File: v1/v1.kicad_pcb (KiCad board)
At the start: 2 copper layers, 50.4 x 44 mm, 54 parts, among them J1 USB_C_Receptacle_USB2.0_16P, Q1 FS8205A, U1 DW01A, U2 MCP73871-2CC, U3 TPS63000, U4 USBLC6-2SC6, U5 SI1016X-T1-GE3, U6 ESP32-WROOM-E, U7 CH340N, Y1 32.768khz

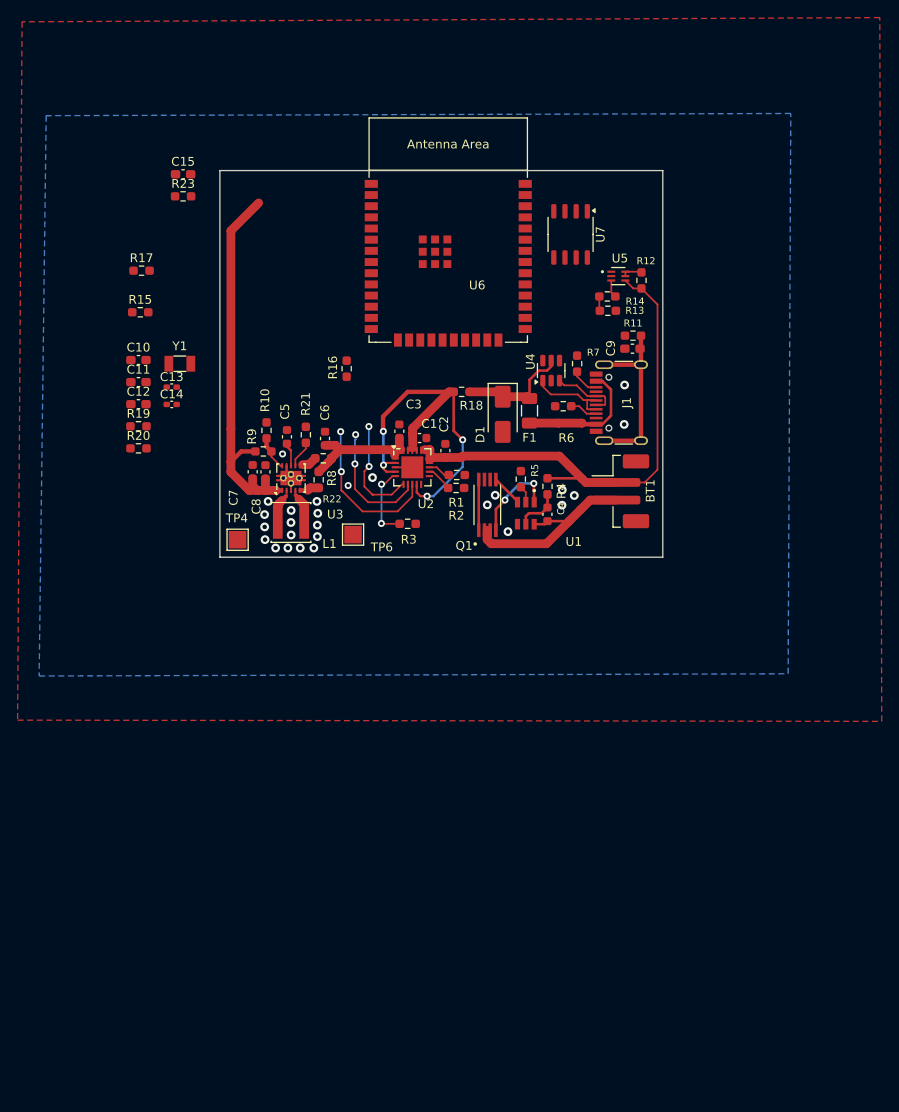
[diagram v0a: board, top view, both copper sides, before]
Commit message: Updated layout
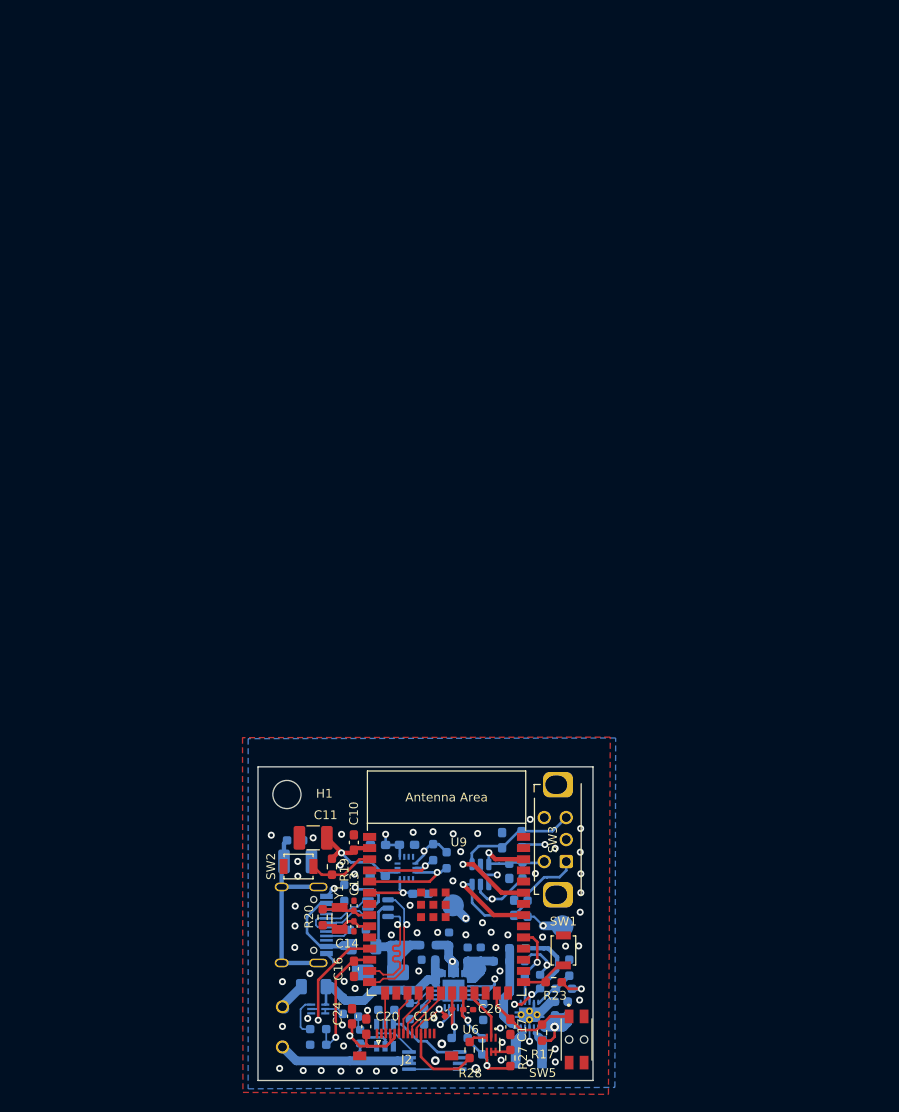
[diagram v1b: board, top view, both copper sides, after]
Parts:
- removed TP4: 3.3v, TestPoint:TestPoint_Pad_2.0x2.0mm
- removed TP6: USB_BAT_AUTO, TestPoint:TestPoint_Pad_2.0x2.0mm
- added C16: 0.1uf, Capacitor_SMD:C_0603_1608Metric_Pad1.08x0.95mm_HandSolder, F.Cu at (115.8, 146.7)
- added C17: 0.1uf, Capacitor_SMD:C_0603_1608Metric_Pad1.08x0.95mm_HandSolder, F.Cu at (133.6, 153.3)
- added C18: 0.1uf, Capacitor_SMD:C_0603_1608Metric_Pad1.08x0.95mm_HandSolder, B.Cu at (133.4, 135.6)
- added C19: 0.1uf, Capacitor_SMD:C_0402_1005Metric_Pad0.74x0.62mm_HandSolder, F.Cu at (126.6, 151.7)
- added C20: 10uf, Capacitor_SMD:C_0603_1608Metric_Pad1.08x0.95mm_HandSolder, F.Cu at (115.6, 152.1)
- added C21: 10uf, Capacitor_SMD:C_0603_1608Metric_Pad1.08x0.95mm_HandSolder, B.Cu at (118.5, 136.2)
- added C22: 0.1uf, Capacitor_SMD:C_0603_1608Metric_Pad1.08x0.95mm_HandSolder, B.Cu at (121.8, 132.6)
- added C23: 0.1uf, Capacitor_SMD:C_0603_1608Metric_Pad1.08x0.95mm_HandSolder, B.Cu at (118.5, 132.7)
- added C24: 0.1uf, Capacitor_SMD:C_0603_1608Metric_Pad1.08x0.95mm_HandSolder, F.Cu at (117.2, 153.3)
- added C25: 0.1uf, Capacitor_SMD:C_0603_1608Metric_Pad1.08x0.95mm_HandSolder, B.Cu at (123.4, 138.2)
- added C26: 0.1uf, Capacitor_SMD:C_0402_1005Metric_Pad0.74x0.62mm_HandSolder, F.Cu at (128.8, 151.4)
- added F2: 1.5A 1206L150THWR, Fuse:Fuse_1206_3216Metric, B.Cu at (111.2, 148.8)
- added G1: GND_TP, TestPoint:TestPoint_Pad_D2.5mm, B.Cu at (127.0, 139.5)
- added H1: MountingHole, MountingHole:MountingHole_3.2mm_M3_ISO14580, F.Cu at (108.2, 126.9)
- added J2: GMT177 Display, Connector_FFC-FPC:TE_1-1734839-3_1x13-1MP_P0.5mm_Horizontal, F.Cu at (121.6, 155.4)
- added P1: 3.3V TP, TestPoint:TestPoint_Pad_D2.5mm, B.Cu at (139.5, 141.9)
- added R24: 10k, Resistor_SMD:R_0603_1608Metric_Pad0.98x0.95mm_HandSolder, B.Cu at (135.5, 139.9)
- added R25: 10k, Resistor_SMD:R_0603_1608Metric_Pad0.98x0.95mm_HandSolder, B.Cu at (134.8, 132.0)
- added R26: 10k, Resistor_SMD:R_0603_1608Metric_Pad0.98x0.95mm_HandSolder, B.Cu at (134.9, 135.6)
- added R27: 10k, Resistor_SMD:R_0603_1608Metric_Pad0.98x0.95mm_HandSolder, F.Cu at (133.6, 156.9)
- added R28: 10, Resistor_SMD:R_0603_1608Metric_Pad0.98x0.95mm_HandSolder, F.Cu at (128.9, 156.0)
- added R29: 10k, Resistor_SMD:R_0603_1608Metric_Pad0.98x0.95mm_HandSolder, B.Cu at (126.3, 134.4)
- added R30: 10k, Resistor_SMD:R_0603_1608Metric_Pad0.98x0.95mm_HandSolder, B.Cu at (124.8, 133.5)
- added SW1: SW_Push, Button_Switch_SMD:SW_SPST_B3U-1000P, F.Cu at (139.6, 144.7)
- added SW2: SW_Push, Button_Switch_SMD:SW_SPST_B3U-1000P, F.Cu at (109.5, 135.1)
- added SW3: RotaryEncoder_Switch, Rotary_Encoder:RotaryEncoder_Bourns_Horizontal_PEC12R-2x17F-Sxxxx, F.Cu at (139.9, 134.5)
- added SW5: Back button, Right angle switch:EVQPUC02K, F.Cu at (141.1, 154.8)
- added U8: BMI270, Package_LGA:Bosch_LGA-14_3x2.5mm_P0.5mm, B.Cu at (121.8, 135.3)
- added U9: ESP32-S3-WROOM-1, PCM_Espressif:ESP32-S3-WROOM-1, F.Cu at (126.3, 140.0)
- BT1: footprint Connector_JST:JST_PH_B2B-PH-SM4-TB_1x02-1MP_P2.00mm_Vertical -> Battery_Library:4.2v_battery_mount; moved to B.Cu
- C1, C12, C15, C2, C3, C4, C5, C6, C7, C8, D1, J1, L1, Q1, R1, R10, R11, R12, R13, R14, R15, R16, R2, R21, R3, R4, R5, R6, R7, R8, R9, U1, U2, U3, U4, U5: moved to B.Cu
- C11: footprint Capacitor_SMD:C_0603_1608Metric_Pad1.08x0.95mm_HandSolder -> Capacitor_SMD:C_1210_3225Metric_Pad1.33x2.70mm_HandSolder
- C9: footprint Capacitor_SMD:C_0603_1608Metric_Pad1.08x0.95mm_HandSolder -> Capacitor_SMD:C_1210_3225Metric_Pad1.33x2.70mm_HandSolder; moved to B.Cu
- F1: value 1A 1206L050YR -> 1.5A 1206L150THWR; moved to B.Cu
- R17: value 100k -> 10k
- R18, R22: value 0.1 -> 0; moved to B.Cu
- U6: value ESP32-WROOM-E -> SI1016X-T1-GE3; footprint PCM_Espressif:ESP32-WROOM-32E -> footprints:SOT_X-T1-GE3_VIS-M
- U7: value CH340N -> SRV05-4; footprint Package_SO:SOP-8_3.9x4.9mm_P1.27mm -> Package_TO_SOT_SMD:SOT-23-6; moved to B.Cu
- moved R23 98.8 mm to (138.5, 148.3)
- moved R17 97.9 mm to (137.2, 154.0), turned to 90 degrees
- moved R15 92.1 mm to (130.4, 155.6), turned to 90 degrees
- moved C15 91.5 mm to (134.0, 139.8), turned to 90 degrees
- moved U6 91.0 mm to (131.4, 155.4), turned to -90 degrees
- moved U5 90.0 mm to (111.7, 151.3)
- moved R13 89.7 mm to (111.7, 155.4), turned to 180 degrees
- moved R14 89.5 mm to (111.7, 153.6), turned to 0 degrees
- moved R12 89.2 mm to (114.5, 151.0), turned to -90 degrees
- moved R16 77.2 mm to (127.8, 154.6), turned to 180 degrees
- moved U7 73.5 mm to (130.2, 136.0)
- moved BT1 71.8 mm to (107.7, 153.1), turned to 90 degrees
- moved J1 70.9 mm to (108.6, 141.8)
- moved C7 70.7 mm to (140.1, 151.2)
- moved R10 70.1 mm to (140.3, 146.6)
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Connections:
- net /Power Module/BATT_LIFE_DATA_ANALOG renamed /MCU/BATT_READ_DATA_ANALOG
- net /Power Module/GPIO_BUCK_BOOST_PS_EN renamed /MCU/PWR_EFFICIENCY_MODE
- BT1 pad 1: /Power Module/B+ -> /Power Module/B-
- BT1 pad 2: /Power Module/B- -> Net-(BT1-+)
- C12 pad 1: Net-(U6-EN/CHIP_PU) -> /MCU/ROTARY_B
- C15 pad 1: GND -> /MCU/ROTARY_A
- C15 pad 2: Net-(U7-V3) -> GND
- D1 pad 1: /MCU/USB_5V -> /Power Module/USB_5V_FUSE_PROT
- F1 pad 2: /MCU/USB_5V -> /Power Module/USB_5V_FUSE_PROT
- R17 pad 2: /Power Module/STAT2 -> Net-(U9-GPIO48/SPICLK_N/SUBSPICLK_N_DIFF)
- R18 pad 1: /MCU/USB_5V -> /Power Module/USB_5V_FUSE_PROT
- R19 pad 2: Net-(U6-EN/CHIP_PU) -> Net-(U9-EN)
- R22 pad 1: /Power Module/AUTO_SWTCH_5V -> /Power Module/AUTO_PATH_PWR
- R22 pad 2: Net-(U3-VIN) -> /Power Module/AUTO_SWTCH_5V
- R23 pad 1: /Power Module/3.3V_PWR -> Net-(U9-GPIO0/BOOT)
- R23 pad 2: Net-(U6-GPIO0/BOOT/ADC2_CH1) -> /Power Module/3.3V_PWR
- R8 pad 1: /Power Module/AUTO_SWTCH_5V -> Net-(U3-EN)
- R8 pad 2: Net-(U3-EN) -> /Power Module/AUTO_PATH_PWR
- U3 pad 5: Net-(U3-VIN) -> /Power Module/AUTO_PATH_PWR
- U4 pad 5: /MCU/USB_5V -> /Power Module/USB_5V_FUSE_PROT
- U5 pad 2: /Power Module/BATT_LIFE_READ_EN -> /MCU/BAT_READ_ENABLE
- U6 pad 2: /Power Module/3.3V_PWR -> /MCU/BACKLIGHT_PWM
- U6 pad 3: Net-(U6-EN/CHIP_PU) -> /MCU/PWM_BACKLT_PWR
- U6 pad 4: unconnected-(U6-SENSOR_VP/GPIO36/ADC1_CH0-Pad4) -> /Power Module/3.3V_PWR
- U6 pad 5: unconnected-(U6-SENSOR_VN/GPIO39/ADC1_CH3-Pad5) -> Net-(U6-D1)
- U6 pad 6: unconnected-(U6-GPIO34/ADC1_CH6-Pad6) -> Net-(U6-D1)
- U7 pad 1: /MCU/PROTECTED_USB_D+ -> /MCU/ROTARY_B
- U7 pad 2: /MCU/PROTECTED_USB_D- -> GND
- U7 pad 3: GND -> /MCU/ROTARY_SW_INT_RTC
- U7 pad 5: /MCU/USB_5V -> /Power Module/3.3V_PWR
- U7 pad 6: /MCU/USB_TX -> /MCU/ROTARY_A
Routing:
- net /Power Module/B+: track 57.1 -> 19.5 mm
- net GND: track 4.74 -> 37.4 mm, vias 26 -> 73
- net /Power Module/3.3V_PWR: track 45.2 -> 77.9 mm, vias 0 -> 10
- net /MCU/ROTARY_A: track 0.00 -> 27.1 mm, vias 0 -> 1
- net /Power Module/USB_5V: track 48.9 -> 22.2 mm, vias 4 -> 3
- net /MCU/ROTARY_B: track 0.00 -> 23.1 mm, vias 0 -> 1
- net /Power Module/USB_5V_FUSE_PROT: track 0.00 -> 21.4 mm
- net /MCU/PROTECTED_USB_D+: track 0.00 -> 14.2 mm, vias 0 -> 1
- net /MCU/PROTECTED_USB_D-: track 0.00 -> 14.1 mm, vias 0 -> 1
- net /Power Module/STAT2: track 14.1 -> 0.00 mm, vias 2 -> 0
- net /MCU/BAT_READ_ENABLE: track 0.00 -> 13.9 mm, vias 0 -> 1
- net /MCU/BATT_READ_DATA_ANALOG: track 1.65 -> 14.7 mm, vias 0 -> 1
- net /MCU/USB_5V: track 13.0 -> 0.00 mm
- net /MCU/ROTARY_SW_INT_RTC: track 0.00 -> 12.4 mm, vias 0 -> 1
- net /MCU/BMI_I2C_SDA: track 0.00 -> 12.4 mm, vias 0 -> 1
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- added copper zone on In2.Cu, net /Power Module/3.3V_PWR
- added copper zone on In2.Cu, net /Power Module/USB_5V
- added copper zone on In1.Cu, net GND
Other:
- board size 50.4 x 44 mm -> 38.1 x 35.7 mm
- copper layers 2 -> 4
- rule solder_mask_min_width: 0.15 -> 0.1
- board text added: "10uf"
- board text added: "L1"
- board text added: "R22"
- board text added: "U3"
